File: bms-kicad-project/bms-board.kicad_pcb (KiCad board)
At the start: 2 copper layers, 49 parts, among them J1 S7B-XH-A, Q1 BSS308PE_H6327, Q2 BSS308PE_H6327, Q3 BSS308PE_H6327, Q5 BSS308PE_H6327, Q6 BSS308PE_H6327, Q7 BSS308PE_H6327, U1 LTC6804-2

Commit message: Feature: Add RP2040 MCU, folder for 3D models of components, continuing edits on other schematics (#15)
* hierarchical label conversion and readability changes

* feat: added minimal MCU schematic, 3D component model folder

* feat:continuing work on integrating RP2040 MCU

* feat: Added 3D models for connector and Flash ROM

* Added 3D Models in Cell Filtering and Balancing Sch.

* feat. Added most 3D models for footprints

* feat: continuing work on MCU circuit

* feat: finished preliminary RP2040 schematic design

---------

Co-authored-by: Dhruv Dingari <dingari.d@northeastern.edu>
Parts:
- R23, R24, R25, R27, R28, R29: value 3K3Ω -> 3k3Ω
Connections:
- C1 pad 2: C0 -> GND
- J1 pad 1: C0 -> GND
- R1 pad 1: C0 -> GND
- R16 pad 1: C0 -> GND
- R9 pad 1: C0 -> GND
- U1 pad 30: C0 -> GND
- U1 pad 31: C0 -> GND
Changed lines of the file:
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@@
   (net 65 "unconnected-(U1-A2-Pad47)")
   (net 66 "unconnected-(U1-A3-Pad48)")
+  (net 67 "GND")
   (footprint "FixedWing:CAPC2012X95N" (layer "F.Cu")
     (at 138.165 71.58)
@@
       (stroke (width 0.1) (type solid)) (layer "F.Fab"))
     (pad "1" smd rect (at -1 0) (size 0.95 1.45) (layers "F.Cu" "F.Paste" "F.Mask")
-      (net 1 "C0") (pinfunction "1") (pintype "passive"))
+      (net 67 "GND") (pinfunction "1") (pintype "passive"))
     (pad "2" smd rect (at 1 0) (size 0.95 1.45) (layers "F.Cu" "F.Paste" "F.Mask")
       (net 1 "C0") (pinfunction "2") (pintype "passive"))
@@
         (effects (font (size 1.27 1.27) (thickness 0.254)))
     )
-    (fp_text value "3K3Ω" (at 0 0) (layer "F.SilkS") hide
+    (fp_text value "3k3Ω" (at 0 0) (layer "F.SilkS") hide
         (effects (font (size 1.27 1.27) (thickness 0.254)))
     )
@@
       (net 1 "C0") (pinfunction "1") (pintype "passive"))
     (pad "2" smd rect (at 0.8 0) (size 1.02 1.47) (layers "F.Cu" "F.Paste" "F.Mask")
-      (net 1 "C0") (pinfunction "2") (pintype "passive"))
+      (net 67 "GND") (pinfunction "2") (pintype "passive"))
     (model "AC0805KRX7R8BB103.stp"
       (offset (xyz 0 0 0))
@@
       (stroke (width 0.508) (type solid)) (fill none) (layer "F.Fab"))
     (pad "1" thru_hole circle (at 0 0) (size 1.4986 1.4986) (drill 0.9906) (layers "*.Cu" "*.Mask")
-      (net 1 "C0") (pinfunction "1") (pintype "unspecified"))
+      (net 67 "GND") (pinfunction "1") (pintype "unspecified"))
     (pad "2" thru_hole circle (at 2.5 0) (size 1.4986 1.4986) (drill 0.9906) (layers "*.Cu" "*.Mask")
       (net 8 "Net-(Q1-S)") (pinfunction "2") (pintype "unspecified"))
@@
         (effects (font (size 1.27 1.27) (thickness 0.254)))
     )
-    (fp_text value "3K3Ω" (at 0 0) (layer "F.SilkS") hide
+    (fp_text value "3k3Ω" (at 0 0) (layer "F.SilkS") hide
         (effects (font (size 1.27 1.27) (thickness 0.254)))
     )
@@
         (effects (font (size 1.27 1.27) (thickness 0.254)))
     )
-    (fp_text value "3K3Ω" (at 0 0) (layer "F.SilkS") hide
+    (fp_text value "3k3Ω" (at 0 0) (layer "F.SilkS") hide
         (effects (font (size 1.27 1.27) (thickness 0.254)))
     )
@@
       (stroke (width 0.1) (type solid)) (layer "F.Fab"))
     (pad "1" smd rect (at -3 0) (size 1.25 3.35) (layers "F.Cu" "F.Paste" "F.Mask")
-      (net 1 "C0") (pinfunction "1") (pintype "passive"))
+      (net 67 "GND") (pinfunction "1") (pintype "passive"))
     (pad "2" smd rect (at 3 0) (size 1.25 3.35) (layers "F.Cu" "F.Paste" "F.Mask")
       (net 15 "Net-(LED1-A)") (pinfunction "2") (pintype "passive"))
@@
       (stroke (width 0.1) (type solid)) (layer "F.Fab"))
     (pad "1" smd rect (at -1 0) (size 0.95 1.45) (layers "F.Cu" "F.Paste" "F.Mask")
-      (net 1 "C0") (pinfunction "1") (pintype "passive"))
+      (net 67 "GND") (pinfunction "1") (pintype "passive"))
     (pad "2" smd rect (at 1 0) (size 0.95 1.45) (layers "F.Cu" "F.Paste" "F.Mask")
       (net 14 "Net-(LED1-K)") (pinfunction "2") (pintype "passive"))
@@
       (net 49 "unconnected-(U1-GPIO3-Pad29)") (pinfunction "GPIO3") (pintype "bidirectional"))
     (pad "30" smd roundrect (at 3.5 3.25) (size 1.9 0.3) (layers "F.Cu" "F.Paste" "F.Mask") (roundrect_rratio 0.25)
-      (net 1 "C0") (pinfunction "V-") (pintype "passive"))
+      (net 67 "GND") (pinfunction "V-") (pintype "passive"))
     (pad "31" smd roundrect (at 3.5 2.75) (size 1.9 0.3) (layers "F.Cu" "F.Paste" "F.Mask") (roundrect_rratio 0.25)
-      (net 1 "C0") (pinfunction "V-") (pintype "passive"))
+      (net 67 "GND") (pinfunction "V-") (pintype "passive"))
     (pad "32" smd roundrect (at 3.5 2.25) (size 1.9 0.3) (layers "F.Cu" "F.Paste" "F.Mask") (roundrect_rratio 0.25)
       (net 50 "unconnected-(U1-GPIO4-Pad32)") (pinfunction "GPIO4") (pintype "bidirectional"))
@@
         (effects (font (size 1.27 1.27) (thickness 0.254)))
     )
-    (fp_text value "3K3Ω" (at 0 0) (layer "F.SilkS") hide
+    (fp_text value "3k3Ω" (at 0 0) (layer "F.SilkS") hide
         (effects (font (size 1.27 1.27) (thickness 0.254)))
     )
@@
         (effects (font (size 1.27 1.27) (thickness 0.254)))
     )
-    (fp_text value "3K3Ω" (at 0 0) (layer "F.SilkS") hide
+    (fp_text value "3k3Ω" (at 0 0) (layer "F.SilkS") hide
         (effects (font (size 1.27 1.27) (thickness 0.254)))
     )
@@
         (effects (font (size 1.27 1.27) (thickness 0.254)))
     )
-    (fp_text value "3K3Ω" (at 0 0) (layer "F.SilkS") hide
-        (effects (font (size 1.27 1.27) (thickness 0.254)))
-    )
+    (fp_text value "3k3Ω" (at 0 0) (layer "F.SilkS") hide
+        (effects (font (size 1.27 1.27) (thickness 0.254)))
+    )

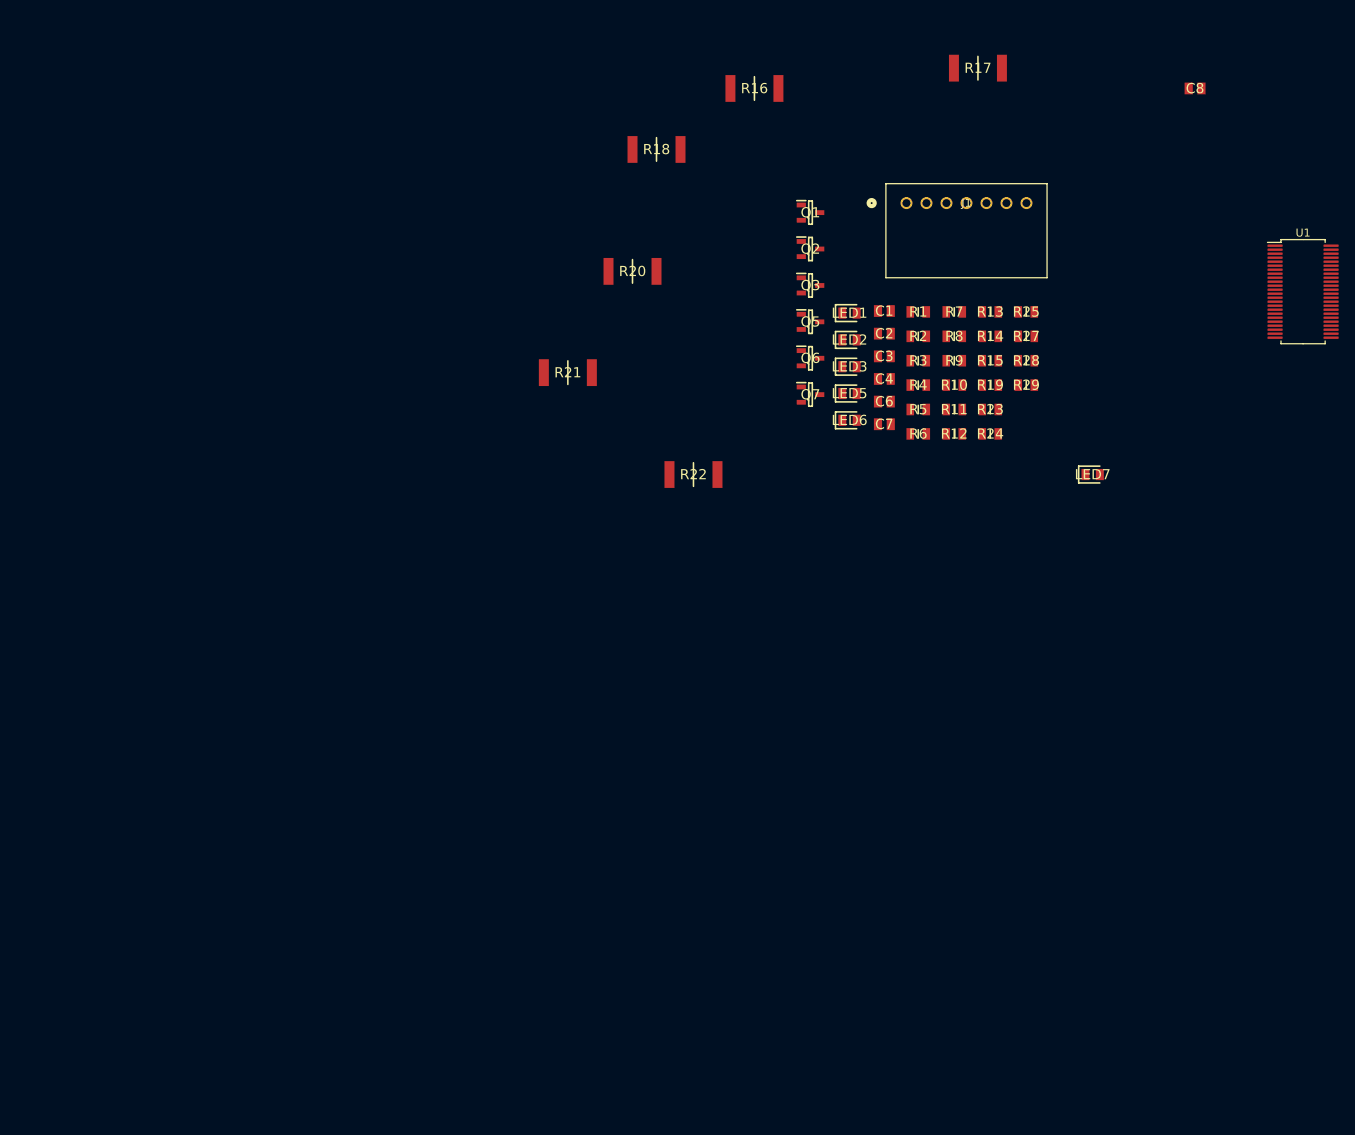
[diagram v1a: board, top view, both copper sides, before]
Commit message: feat: put filtering and balancing circuits into hierarchical format
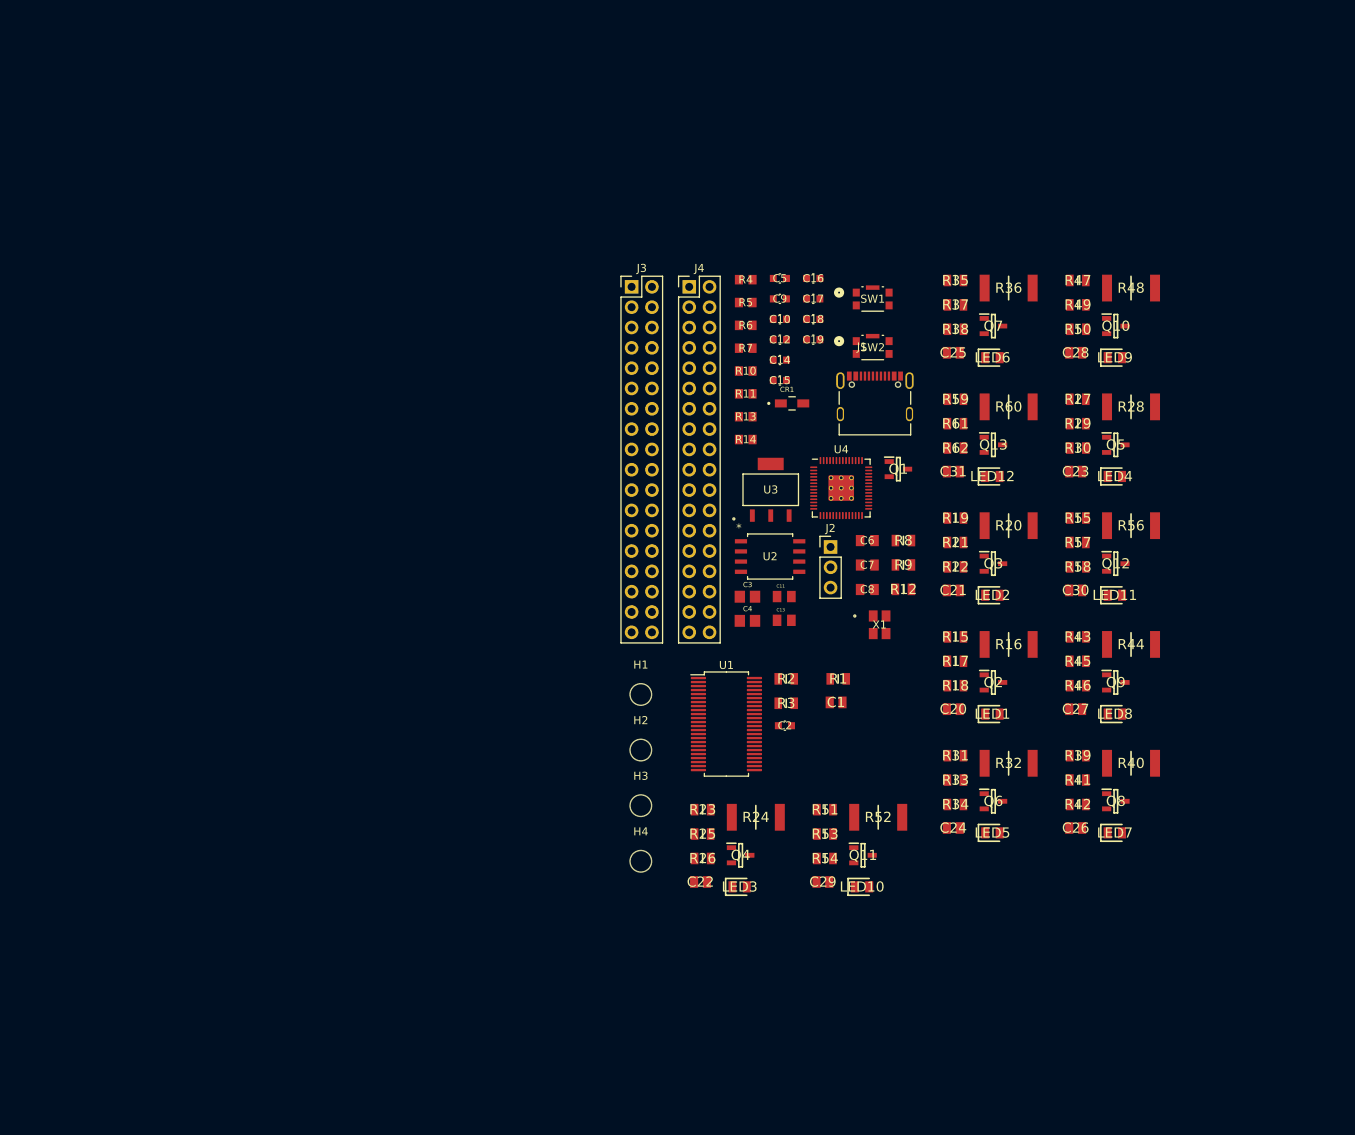
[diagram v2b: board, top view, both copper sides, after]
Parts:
- added C10: 0.1µ, FixedWing:CAP_GCJ-18_MUR, F.Cu at (125.1, 66.9)
- added C11: 1µ, FixedWing:CAPC2012X140N, F.Cu at (125.6, 101.6)
- added C12: 0.1µ, FixedWing:CAP_GCJ-18_MUR, F.Cu at (125.1, 69.5)
- added C13: 1µ, FixedWing:CAPC2012X140N, F.Cu at (125.6, 104.6)
- added C14: 0.1µ, FixedWing:CAP_GCJ-18_MUR, F.Cu at (125.1, 72.0)
- added C15: 0.1µ, FixedWing:CAP_GCJ-18_MUR, F.Cu at (125.1, 74.6)
- added C16: 0.1µ, FixedWing:CAP_GCJ-18_MUR, F.Cu at (129.3, 61.8)
- added C17: 0.1µ, FixedWing:CAP_GCJ-18_MUR, F.Cu at (129.3, 64.4)
- added C18: 0.1µ, FixedWing:CAP_GCJ-18_MUR, F.Cu at (129.3, 66.9)
- added C19: 0.1µ, FixedWing:CAP_GCJ-18_MUR, F.Cu at (129.3, 69.5)
- added C20: 10n, FixedWing:CAPC2012X95N, F.Cu at (146.8, 115.7)
- added C21: 10n, FixedWing:CAPC2012X95N, F.Cu at (146.8, 100.8)
- added C22: 10n, FixedWing:CAPC2012X95N, F.Cu at (115.2, 137.3)
- added C23: 10n, FixedWing:CAPC2012X95N, F.Cu at (162.1, 86.0)
- added C24: 10n, FixedWing:CAPC2012X95N, F.Cu at (146.8, 130.5)
- added C25: 10n, FixedWing:CAPC2012X95N, F.Cu at (146.8, 71.1)
- added C26: 10n, FixedWing:CAPC2012X95N, F.Cu at (162.1, 130.5)
- added C27: 10n, FixedWing:CAPC2012X95N, F.Cu at (162.1, 115.7)
- added C28: 10n, FixedWing:CAPC2012X95N, F.Cu at (162.1, 71.1)
- added C29: 10n, FixedWing:CAPC2012X95N, F.Cu at (130.5, 137.3)
- added C30: 10n, FixedWing:CAPC2012X95N, F.Cu at (162.1, 100.8)
- added C31: 10n, FixedWing:CAPC2012X95N, F.Cu at (146.8, 86.0)
- added C5: 0.1µ, FixedWing:CAP_GCJ-18_MUR, F.Cu at (125.1, 61.8)
- added C9: 0.1µ, FixedWing:CAP_GCJ-18_MUR, F.Cu at (125.1, 64.4)
- added CR1: MBR120VLSFT1G, FixedWing:DIOM3616X98N, F.Cu at (126.6, 77.5)
- added H1: MountingHole, MountingHole:MountingHole_2.7mm_M2.5, F.Cu at (107.7, 113.8)
- added H2: MountingHole, MountingHole:MountingHole_2.7mm_M2.5, F.Cu at (107.7, 120.8)
- added H3: MountingHole, MountingHole:MountingHole_2.7mm_M2.5, F.Cu at (107.7, 127.8)
- added H4: MountingHole, MountingHole:MountingHole_2.7mm_M2.5, F.Cu at (107.7, 134.7)
- added J2: DEBUG, Connector_PinHeader_2.54mm:PinHeader_1x03_P2.54mm_Vertical, F.Cu at (131.4, 95.4)
- added J3: Conn_02x18_Odd_Even, Connector_PinHeader_2.54mm:PinHeader_2x18_P2.54mm_Vertical, F.Cu at (106.6, 62.9)
- added J4: Conn_02x18_Odd_Even, Connector_PinHeader_2.54mm:PinHeader_2x18_P2.54mm_Vertical, F.Cu at (113.8, 62.9)
- added LED10: LTST-C170KRKT, FixedWing:LEDC2012X120N, F.Cu at (135.4, 137.9)
- added LED11: LTST-C170KRKT, FixedWing:LEDC2012X120N, F.Cu at (167.0, 101.5)
- added LED12: LTST-C170KRKT, FixedWing:LEDC2012X120N, F.Cu at (151.7, 86.6)
- added LED4: LTST-C170KRKT, FixedWing:LEDC2012X120N, F.Cu at (167.0, 86.6)
- added LED8: LTST-C170KRKT, FixedWing:LEDC2012X120N, F.Cu at (167.0, 116.3)
- added LED9: LTST-C170KRKT, FixedWing:LEDC2012X120N, F.Cu at (167.0, 71.8)
- added Q10: BSS308PE_H6327, FixedWing:SOT95P260X110-3N, F.Cu at (167.1, 67.8)
- added Q11: BSS308PE_H6327, FixedWing:SOT95P260X110-3N, F.Cu at (135.5, 133.9)
- added Q12: BSS308PE_H6327, FixedWing:SOT95P260X110-3N, F.Cu at (167.1, 97.5)
- added Q13: BSS308PE_H6327, FixedWing:SOT95P260X110-3N, F.Cu at (151.8, 82.7)
- added Q4: BSS308PE_H6327, FixedWing:SOT95P260X110-3N, F.Cu at (120.2, 133.9)
- added Q8: BSS308PE_H6327, FixedWing:SOT95P260X110-3N, F.Cu at (167.1, 127.2)
- added Q9: BSS308PE_H6327, FixedWing:SOT95P260X110-3N, F.Cu at (167.1, 112.3)
- added R26: 3k3, FixedWing:RESC2012X50N, F.Cu at (115.4, 134.3)
- added R30: 3k3, FixedWing:RESC2012X50N, F.Cu at (162.3, 83.0)
- added R31: 475, FixedWing:RESC2012X50N, F.Cu at (147.0, 121.5)
- added R32: 33, FixedWing:RESC6332X70N, F.Cu at (153.7, 122.5)
- added R33: 100, FixedWing:RESC2012X50N, F.Cu at (147.0, 124.5)
- added R34: 3k3, FixedWing:RESC2012X50N, F.Cu at (147.0, 127.6)
- added R35: 475, FixedWing:RESC2012X50N, F.Cu at (147.0, 62.1)
- added R36: 33, FixedWing:RESC6332X70N, F.Cu at (153.7, 63.0)
- added R37: 100, FixedWing:RESC2012X50N, F.Cu at (147.0, 65.2)
- added R38: 3k3, FixedWing:RESC2012X50N, F.Cu at (147.0, 68.2)
- added R39: 475, FixedWing:RESC2012X50N, F.Cu at (162.3, 121.5)
- added R40: 33, FixedWing:RESC6332X70N, F.Cu at (169.0, 122.5)
- added R41: 100, FixedWing:RESC2012X50N, F.Cu at (162.3, 124.5)
- added R42: 3k3, FixedWing:RESC2012X50N, F.Cu at (162.3, 127.6)
- added R43: 475, FixedWing:RESC2012X50N, F.Cu at (162.3, 106.7)
- added R44: 33, FixedWing:RESC6332X70N, F.Cu at (169.0, 107.6)
- added R45: 100, FixedWing:RESC2012X50N, F.Cu at (162.3, 109.7)
- added R46: 3k3, FixedWing:RESC2012X50N, F.Cu at (162.3, 112.8)
- added R47: 475, FixedWing:RESC2012X50N, F.Cu at (162.3, 62.1)
- added R48: 33, FixedWing:RESC6332X70N, F.Cu at (169.0, 63.0)
- added R49: 100, FixedWing:RESC2012X50N, F.Cu at (162.3, 65.2)
- added R50: 3k3, FixedWing:RESC2012X50N, F.Cu at (162.3, 68.2)
- added R51: 475, FixedWing:RESC2012X50N, F.Cu at (130.7, 128.2)
- added R52: 33, FixedWing:RESC6332X70N, F.Cu at (137.4, 129.2)
- added R53: 100, FixedWing:RESC2012X50N, F.Cu at (130.7, 131.3)
- added R54: 3k3, FixedWing:RESC2012X50N, F.Cu at (130.7, 134.3)
- added R55: 475, FixedWing:RESC2012X50N, F.Cu at (162.3, 91.8)
- added R56: 33, FixedWing:RESC6332X70N, F.Cu at (169.0, 92.8)
- added R57: 100, FixedWing:RESC2012X50N, F.Cu at (162.3, 94.8)
- added R58: 3k3, FixedWing:RESC2012X50N, F.Cu at (162.3, 97.9)
- added R59: 475, FixedWing:RESC2012X50N, F.Cu at (147.0, 77.0)
- added R60: 33, FixedWing:RESC6332X70N, F.Cu at (153.7, 77.9)
- added R61: 100, FixedWing:RESC2012X50N, F.Cu at (147.0, 80.0)
- added R62: 3k3, FixedWing:RESC2012X50N, F.Cu at (147.0, 83.0)
- added SW1: KMR223G LFG, FixedWing:KMR2_G_CNK, F.Cu at (136.7, 64.4)
- added SW2: KMR223G LFG, FixedWing:KMR2_G_CNK, F.Cu at (136.7, 70.5)
- added U2: W25Q128JVSIQ TR, FixedWing:SOIC_208MIL_WIN, F.Cu at (123.9, 96.6)
- added U3: NCP1117ST33T3G, FixedWing:SOT223-3_ONS, F.Cu at (124.0, 88.3)
- added U4: RP2040, FixedWing:RP2040-QFN-56, F.Cu at (132.8, 88.0)
- added X1: ABM8-272-T3, FixedWing:ABM8-272-T3_ABR, F.Cu at (137.6, 105.1)
- C1: value 10nF -> 10n
- C2: value 10nF -> 0.1µ; footprint FixedWing:CAPC2012X95N -> FixedWing:CAP_GCJ-18_MUR
- C3, C4: value 10nF -> 15p; footprint FixedWing:CAPC2012X95N -> FixedWing:CAPC2012X70
- C6, C7, C8: value 10nF -> 10µ; footprint FixedWing:CAPC2012X95N -> FixedWing:CAP_CL21B106KOQNNNE_SAM
- J1: value S7B-XH-A -> 12402012E212A; footprint FixedWing:CONN_S7B-XH-A_JST -> FixedWing:AMPHENOL_12402012E212A
- R1, R3: value 100Ω -> 100
- R10, R11: value 475Ω -> 1k; footprint FixedWing:RESC2012X50N -> FixedWing:RC0805N_YAG
- R12, R2, R8: value 100Ω -> 3k3
- R13, R14: value 475Ω -> 27; footprint FixedWing:RESC2012X50N -> FixedWing:RC0805N_YAG
- R15: value 475Ω -> 475
- R16, R20: value 33Ω -> 33
- R17, R21: value 33Ω -> 100; footprint FixedWing:RESC6332X70N -> FixedWing:RESC2012X50N
- R18, R22: value 33Ω -> 3k3; footprint FixedWing:RESC6332X70N -> FixedWing:RESC2012X50N
- R19: value 100Ω -> 475
- R23, R27: value 3k3Ω -> 475
- R24, R28: value 3k3Ω -> 33; footprint FixedWing:RESC2012X50N -> FixedWing:RESC6332X70N
- R25, R29: value 3k3Ω -> 100
- R4, R5, R6, R7: value 100Ω -> 1k; footprint FixedWing:RESC2012X50N -> FixedWing:RC0805N_YAG
- R9: value 475Ω -> 3k3
- U1: footprint Package_SO:SSOP-48_5.3x12.8mm_P0.5mm -> FixedWing:SSOP-48_5.3x12.8mm_P0.5mm
- moved U1 90.1 mm to (118.4, 117.5)
- moved R25 76.8 mm to (115.4, 131.3)
- moved R18 76.7 mm to (147.0, 112.8)
- moved R16 76.4 mm to (153.7, 107.6)
- moved C8 74.8 mm to (136.0, 100.7)
- moved R17 74.2 mm to (147.0, 109.7)
- moved LED3 66.5 mm to (120.1, 137.9)
- moved R23 61.6 mm to (115.4, 128.2)
- moved Q6 59.9 mm to (151.8, 127.2)
- moved Q2 58.8 mm to (151.8, 112.3)
- moved LED5 57.8 mm to (151.7, 131.2)
- moved R20 56.8 mm to (153.7, 92.8)
- moved R24 56.2 mm to (122.1, 129.2)
- moved LED1 53.2 mm to (151.7, 116.3)
- moved R21 52.9 mm to (147.0, 94.8)
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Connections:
- C1 pad 1: C0 -> /Battery Stack Monitor/C0
- C2 pad 1: C1 -> Net-(U1-V+)
- C2 pad 2: C0 -> GND
- C3 pad 1: C2 -> GND
- C3 pad 2: C1 -> /RP2040 Microcontroller/XIN
- C4 pad 1: C3 -> GND
- C4 pad 2: C2 -> Net-(C4-Pad2)
- C6 pad 1: C7 -> GND
- C6 pad 2: C3 -> Net-(Q1-S)
- C7 pad 1: C8 -> +3V3
- C7 pad 2: C7 -> GND
- C8 pad 1: C9 -> GND
- C8 pad 2: C8 -> +3V3
- Q1 pad 1: Net-(Q1-G) -> Net-(J1-VBUS)
- Q1 pad 3: Net-(LED1-A) -> +5V
- Q2 pad 2: Net-(Q2-S) -> /Cell Filtering and Balancing/Filter and Balance Cell 1/BATT(n)
- Q2 pad 3: Net-(LED2-A) -> Net-(LED1-A)
- Q3 pad 2: Net-(Q3-S) -> /Cell Filtering and Balancing/Filter and Balance Cell 2/BATT(n)
- Q3 pad 3: Net-(LED3-A) -> Net-(LED2-A)
- Q5 pad 2: Net-(Q5-S) -> /Cell Filtering and Balancing/Filter and Balance Cell 4/BATT(n)
- Q5 pad 3: Net-(LED5-A) -> Net-(LED4-A)
- Q6 pad 2: Net-(Q6-S) -> /Cell Filtering and Balancing/Filter and Balance Cell 5/BATT(n)
- Q6 pad 3: Net-(LED6-A) -> Net-(LED5-A)
- Q7 pad 2: Net-(Q7-S) -> /Cell Filtering and Balancing/Filter and Balance Cell 6/BATT(n)
- Q7 pad 3: Net-(LED7-A) -> Net-(LED6-A)
- R1 pad 1: GND -> /Cell Filtering and Balancing/Filter and Balance Cell 12/BATT(n)
- R1 pad 2: C0 -> /Battery Stack Monitor/C12
- R10 pad 1: Net-(Q1-S) -> Net-(C4-Pad2)
- R10 pad 2: Net-(LED2-K) -> /RP2040 Microcontroller/XOUT
- R11 pad 1: Net-(Q2-S) -> /RP2040 Microcontroller/~{USB_BOOT}
- R11 pad 2: Net-(LED3-K) -> /RP2040 Microcontroller/QSPI_SS
- R12 pad 1: Net-(Q7-S) -> /RP2040 Microcontroller/~{RESET}
- R12 pad 2: C12 -> +3V3
- R13 pad 1: Net-(Q3-S) -> Net-(U4-USB_DP)
- R13 pad 2: Net-(LED5-K) -> /RP2040 Microcontroller/USB_D+
- R14 pad 1: Net-(Q5-S) -> Net-(U4-USB_DM)
- R14 pad 2: Net-(LED6-K) -> /RP2040 Microcontroller/USB_D-
- R15 pad 1: Net-(Q6-S) -> GND
- R15 pad 2: Net-(LED7-K) -> Net-(LED1-K)
- R17 pad 1: Net-(Q1-S) -> GND
- R17 pad 2: Net-(LED2-A) -> /Battery Stack Monitor/C0
- R18 pad 1: Net-(Q2-S) -> /Battery Stack Monitor/S1
- R18 pad 2: Net-(LED3-A) -> Net-(Q2-G)
- R19 pad 1: Net-(Q7-S) -> /Cell Filtering and Balancing/Filter and Balance Cell 1/BATT(n)
- R19 pad 2: VIN_MONITOR -> Net-(LED2-K)
- R2 pad 1: Net-(Q1-S) -> /RP2040 Microcontroller/GPIO0
- R2 pad 2: C1 -> +5V
- R20 pad 1: Net-(Q3-S) -> /Cell Filtering and Balancing/Filter and Balance Cell 1/BATT(n)
- R20 pad 2: Net-(LED5-A) -> Net-(LED2-A)
- R21 pad 1: Net-(Q5-S) -> /Cell Filtering and Balancing/Filter and Balance Cell 1/BATT(n)
- R21 pad 2: Net-(LED6-A) -> /Battery Stack Monitor/C1
- R22 pad 1: Net-(Q6-S) -> /Battery Stack Monitor/S2
- R22 pad 2: Net-(LED7-A) -> Net-(Q3-G)
- R23 pad 1: S1 -> /Cell Filtering and Balancing/Filter and Balance Cell 2/BATT(n)
- R23 pad 2: Net-(Q1-G) -> Net-(LED3-K)
- R24 pad 1: S2 -> /Cell Filtering and Balancing/Filter and Balance Cell 2/BATT(n)
- R24 pad 2: Net-(Q2-G) -> Net-(LED3-A)
- R25 pad 1: S3 -> /Cell Filtering and Balancing/Filter and Balance Cell 2/BATT(n)
- R25 pad 2: Net-(Q3-G) -> /Battery Stack Monitor/C2
- R27 pad 1: S7 -> /Cell Filtering and Balancing/Filter and Balance Cell 3/BATT(n)
- R27 pad 2: Net-(Q5-G) -> Net-(LED4-K)
- R28 pad 1: S8 -> /Cell Filtering and Balancing/Filter and Balance Cell 3/BATT(n)
- R28 pad 2: Net-(Q6-G) -> Net-(LED4-A)
- R29 pad 1: S9 -> /Cell Filtering and Balancing/Filter and Balance Cell 3/BATT(n)
- R29 pad 2: Net-(Q7-G) -> /Battery Stack Monitor/C3
- R3 pad 1: Net-(Q2-S) -> Net-(U1-V+)
- R3 pad 2: C2 -> +BATT
- R4 pad 1: Net-(Q3-S) -> Net-(R4-Pad1)
- R4 pad 2: C3 -> GND
- R5 pad 1: Net-(Q3-S) -> Net-(R5-Pad1)
- R5 pad 2: C6 -> GND
- R6 pad 1: Net-(Q5-S) -> Net-(R6-Pad1)
- R6 pad 2: C7 -> Net-(R4-Pad1)
- R7 pad 1: Net-(Q6-S) -> Net-(R7-Pad1)
- R7 pad 2: C8 -> Net-(R5-Pad1)
- R8 pad 1: Net-(Q7-S) -> Net-(J1-CC1_B)
- R8 pad 2: C9 -> Net-(R6-Pad1)
- R9 pad 1: GND -> Net-(J1-CC1_A)
- R9 pad 2: Net-(LED1-K) -> Net-(R7-Pad1)
- U1 pad 1: VIN_MONITOR -> Net-(U1-V+)
- U1 pad 10: C8 -> /Battery Stack Monitor/C8
- U1 pad 11: S8 -> /Battery Stack Monitor/S8
- U1 pad 12: C7 -> /Battery Stack Monitor/C7
- U1 pad 13: S7 -> /Battery Stack Monitor/S7
- U1 pad 14: C6 -> /Battery Stack Monitor/C6
- U1 pad 16: C6 -> /Battery Stack Monitor/C6
- U1 pad 18: C6 -> /Battery Stack Monitor/C6
- U1 pad 2: C12 -> /Battery Stack Monitor/C12
- U1 pad 20: C3 -> /Battery Stack Monitor/C3
- U1 pad 21: S3 -> /Battery Stack Monitor/S3
- U1 pad 22: C2 -> /Battery Stack Monitor/C2
- U1 pad 23: S2 -> /Battery Stack Monitor/S2
- U1 pad 24: C1 -> /Battery Stack Monitor/C1
- U1 pad 25: S1 -> /Battery Stack Monitor/S1
- U1 pad 26: C0 -> /Battery Stack Monitor/C0
- U1 pad 37: unconnected-(U1-VREG-Pad37) -> +5V
- U1 pad 4: C12 -> /Battery Stack Monitor/C12
- U1 pad 40: unconnected-(U1-ISOMD-Pad40) -> GND
- U1 pad 41: unconnected-(U1-CSB(IMA)-Pad41) -> /RP2040 Microcontroller/GPIO1
- U1 pad 42: unconnected-(U1-SCK(IPA)-Pad42) -> /RP2040 Microcontroller/GPIO2
- U1 pad 43: unconnected-(U1-SDI(ICMP)-Pad43) -> /RP2040 Microcontroller/GPIO3
- U1 pad 44: unconnected-(U1-SDO(IBIAS)-Pad44) -> /RP2040 Microcontroller/GPIO0
- U1 pad 6: C12 -> /Battery Stack Monitor/C12
- U1 pad 8: C9 -> /Battery Stack Monitor/C9
- U1 pad 9: S9 -> /Battery Stack Monitor/S9

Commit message: feat: forgot to commit smol change
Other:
- copper layers 2 -> 4
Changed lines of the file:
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@@
 (kicad_pcb (version 20221018) (generator pcbnew)
   (general
-    (thickness 1.6)
+    (thickness 1.67)
   )
   (paper "A")
   (layers
     (0 "F.Cu" signal)
+    (1 "In1.Cu" signal)
+    (2 "In2.Cu" signal)
     (31 "B.Cu" signal)
     (32 "B.Adhes" user "B.Adhesive")
@@
   )
   (setup
+    (stackup
+      (layer "F.SilkS" (type "Top Silk Screen"))
+      (layer "F.Paste" (type "Top Solder Paste"))
+      (layer "F.Mask" (type "Top Solder Mask") (thickness 0.01))
+      (layer "F.Cu" (type "copper") (thickness 0.07))
+      (layer "dielectric 1" (type "prepreg") (thickness 0.1) (material "FR4") (epsilon_r 4.5) (loss_tangent 0.02))
+      (layer "In1.Cu" (type "copper") (thickness 0.035))
+      (layer "dielectric 2" (type "prepreg") (thickness 1.24) (material "FR4") (epsilon_r 4.5) (loss_tangent 0.02))
+      (layer "In2.Cu" (type "copper") (thickness 0.035))
+      (layer "dielectric 3" (type "prepreg") (thickness 0.1) (material "FR4") (epsilon_r 4.5) (loss_tangent 0.02))
+      (layer "B.Cu" (type "copper") (thickness 0.07))
+      (layer "B.Mask" (type "Bottom Solder Mask") (thickness 0.01))
+      (layer "B.Paste" (type "Bottom Solder Paste"))
+      (layer "B.SilkS" (type "Bottom Silk Screen"))
+      (copper_finish "None")
+      (dielectric_constraints no)
+    )
     (pad_to_mask_clearance 0)
     (pcbplotparams
